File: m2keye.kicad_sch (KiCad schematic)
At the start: 0 parts

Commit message: [#56643] Create buses for interfaces, assign buses to blocks
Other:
- company: (none) -> Antmicro Ltd.
- title: (none) -> Com Express 7 baseboard
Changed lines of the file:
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@@
 (kicad_sch (version 20230121) (generator eeschema)
-  (paper "A4")
+  (paper "A3")
+  (title_block
+    (title "Com Express 7 baseboard")
+    (date "2024-03-22")
+    (rev "1.0.0")
+    (company "Antmicro Ltd.")
+  )
   (hierarchical_label "USB{USB}" (shape input) (at 66.04 81.28 180) (fields_autoplaced)
     (effects (font (size 1.27 1.27)) (justify right))

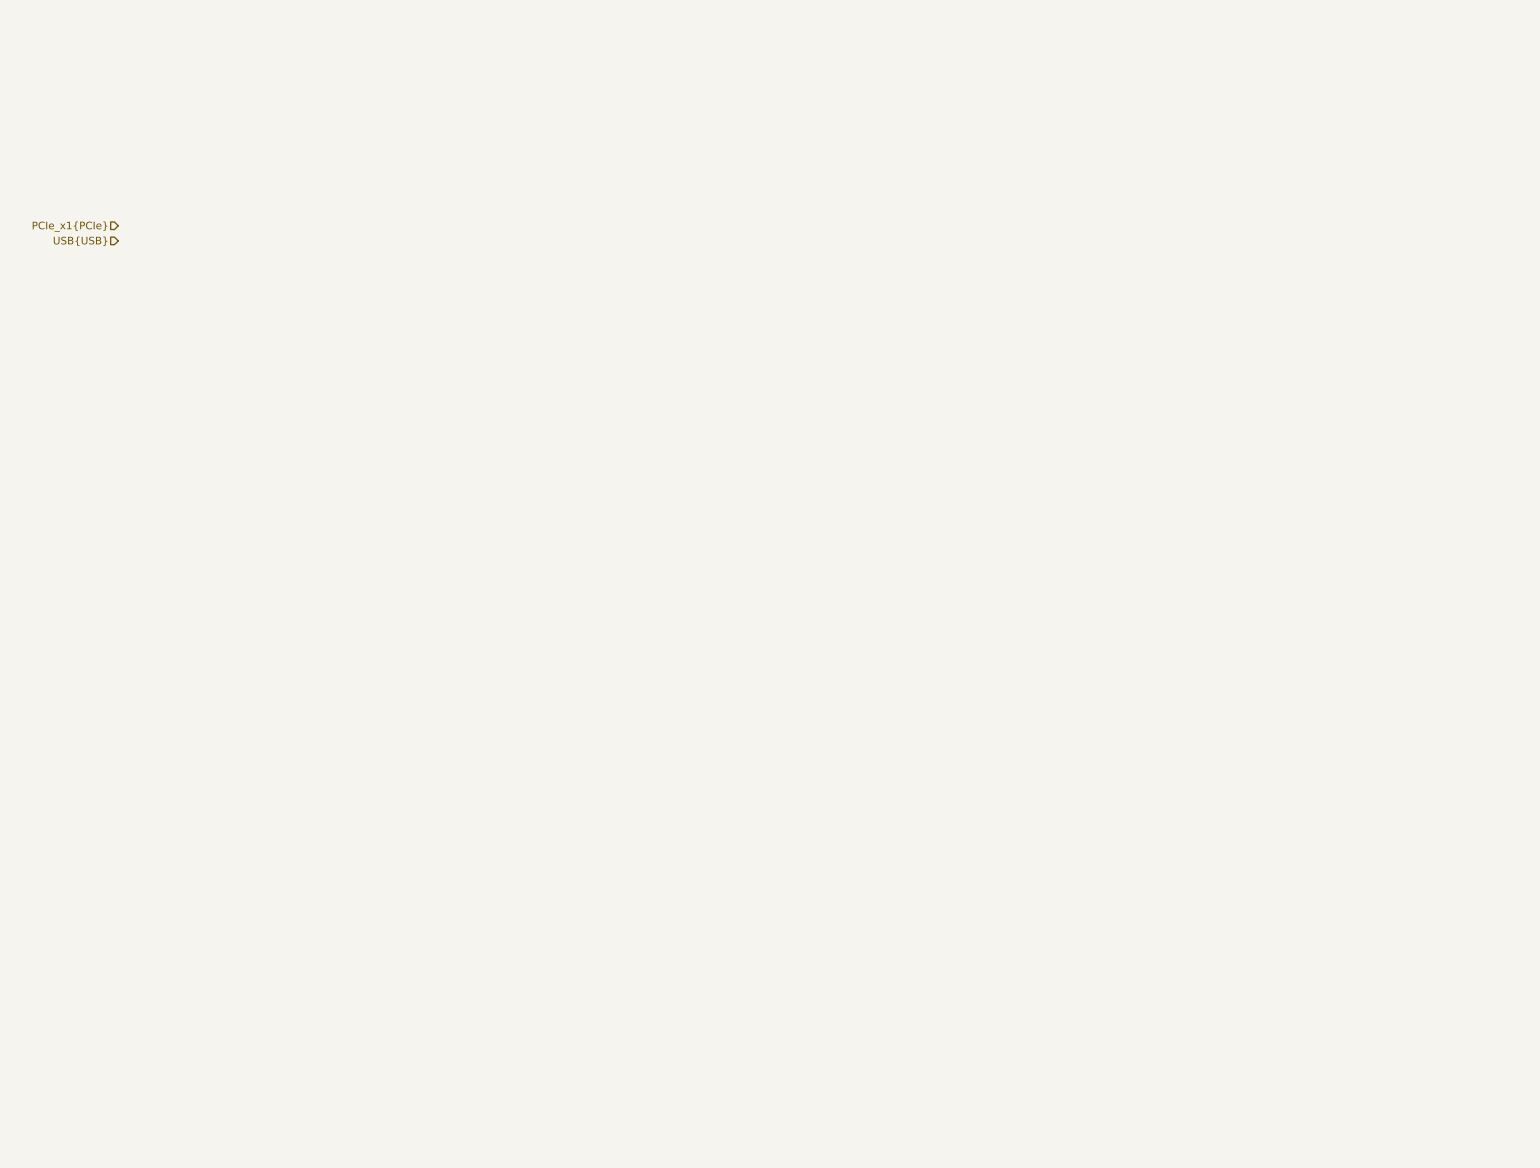
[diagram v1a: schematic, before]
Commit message: [#57056] Create schematics for M.2 and OCuLink connectors
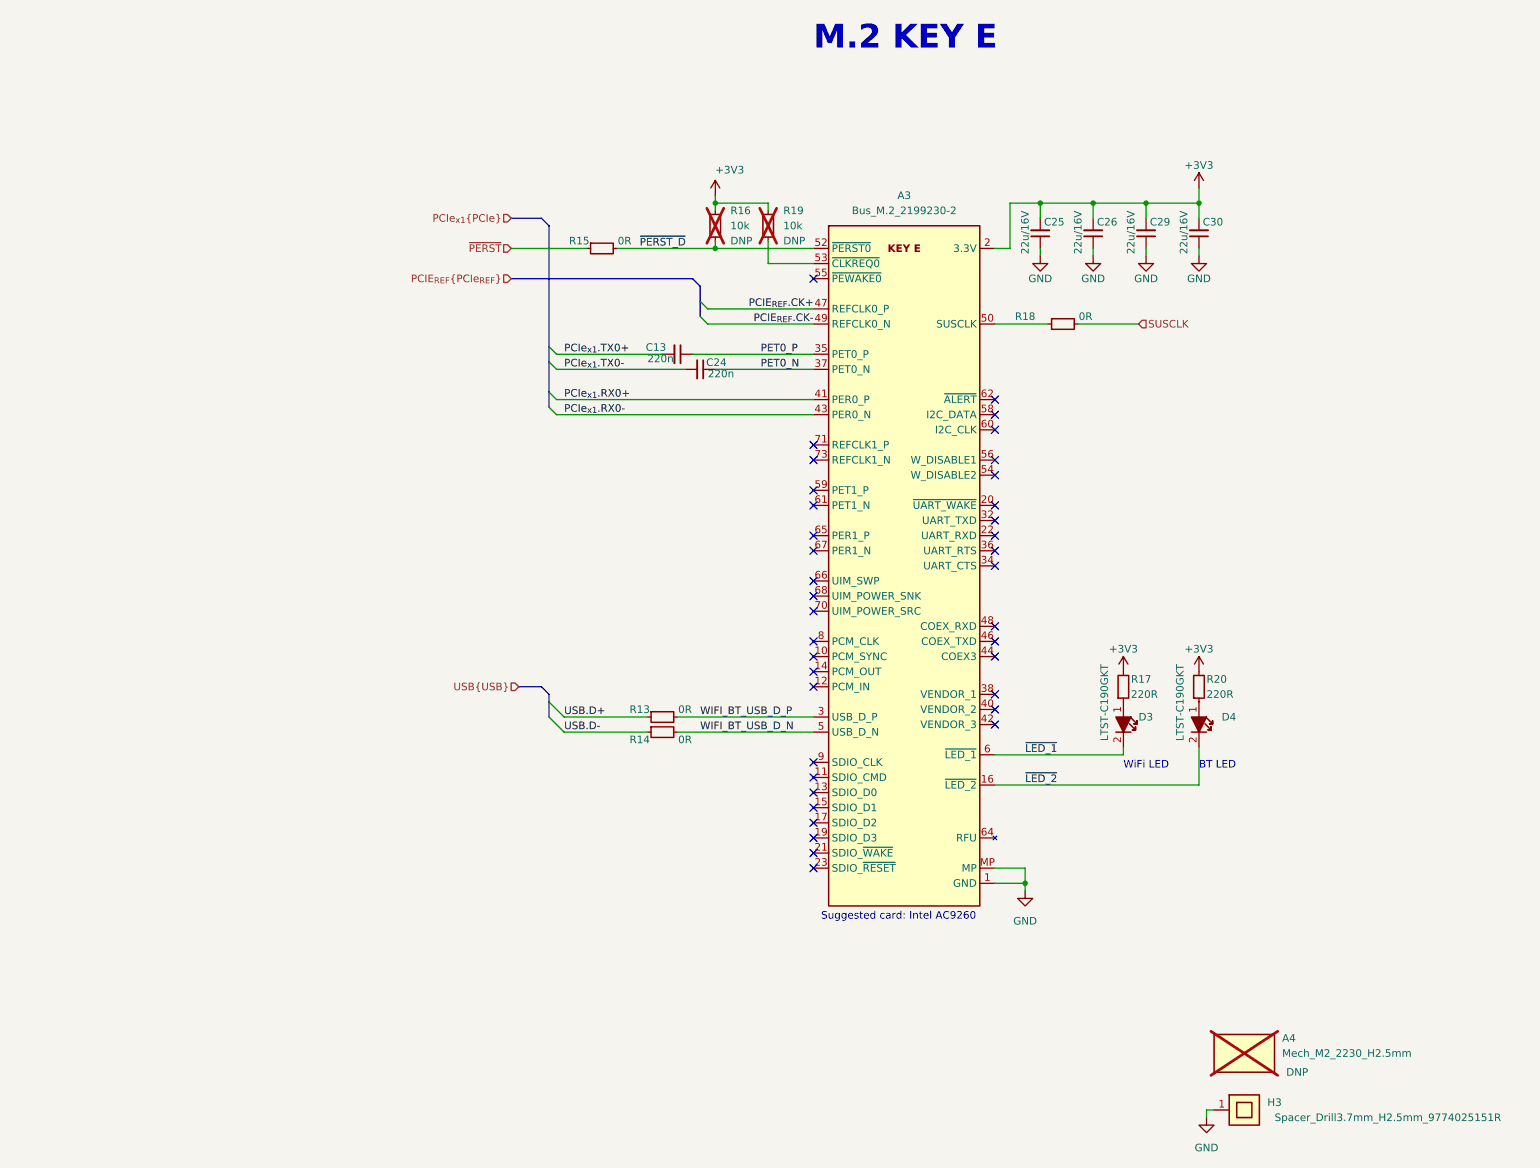
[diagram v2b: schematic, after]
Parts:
- added A3: Bus_M.2_2199230-2, antmicro-footprints:Bus_M.2_Socket_Key_E_TE_2199230-6, symbol antmicroPciConnectors:Bus_M.2_2199230-2
- added A4: Mech_M2_2230_H2.5mm, antmicro-footprints:Mech_M2_2230_H2.5mm, symbol antmicroModules:Mech_M2_2230_H2.5mm
- added C13, C24: C_220n_0402, antmicro-footprints:C_0402_1005Metric, symbol antmicroCapacitors0402:C_220n_0402
- added C25, C26, C29, C30: C_22u_16V_0603, antmicro-footprints:C_0603_1608Metric, symbol antmicroCapacitors0603:C_22u_16V_0603
- added D3, D4: LED_G_0603_LTST-C190GKT, antmicro-footprints:LED_0603_1608Metric_G, symbol antmicroLEDIndicationDiscrete:LED_G_0603_LTST-C190GKT
- added H3: Spacer_Drill3.7mm_H2.5mm_9774025151R, antmicro-footprints:Spacer_Drill3.7mm_H2.5mm_9774025151R, symbol antmicroMechanicalParts:Spacer_Drill3.7mm_H2.5mm_9774025151R
- added R13, R14, R15, R18: R_0R_0402, antmicro-footprints:R_0402_1005Metric, symbol antmicroResistors0402:R_0R_0402
- added R16, R19: R_10k_0402, antmicro-footprints:R_0402_1005Metric, symbol antmicroResistors0402:R_10k_0402
- added R17, R20: R_220R_0402, antmicro-footprints:R_0402_1005Metric, symbol antmicroResistors0402:R_220R_0402
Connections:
- new net: D3.1, R17.1
- new net: A3.50 (SUSCLK), R18.1
- new net: A3.53 (~{CLKREQ0}), R19.1
- new net: D4.1, R20.1
- new net +3V3: A3.2 (3.3V), A3.4 (3.3V), A3.72 (3.3V), A3.74 (3.3V), C25.2, C26.2, C29.2, C30.2, R16.2, R17.2, R19.2, R20.2
- new net GND: A3.1 (GND), A3.18 (GND), A3.33 (GND), A3.39 (GND), A3.45 (GND), A3.51 (GND), A3.57 (GND), A3.63 (GND), A3.69 (GND), A3.7 (GND), A3.75 (GND), A3.MP, C25.1, C26.1, C29.1, C30.1, H3.1
- new net PCIE_{REF}.CK+: A3.47 (REFCLK0_P)
- new net PCIE_{REF}.CK-: A3.49 (REFCLK0_N)
- new net PCIe_{x1}.RX0+: A3.41 (PER0_P)
- new net PCIe_{x1}.RX0-: A3.43 (PER0_N)
- new net PCIe_{x1}.TX0+: C13.2
- new net PCIe_{x1}.TX0-: C24.2
- new net PET0_N: A3.37 (PET0_N), C24.1
- new net PET0_P: A3.35 (PET0_P), C13.1
- new net SUSCLK: R18.2
- new net USB.D+: R13.1
- new net USB.D-: R14.1
- new net WIFI_BT_USB_D_N: A3.5 (USB_D_N), R14.2
- new net WIFI_BT_USB_D_P: A3.3 (USB_D_P), R13.2
- new net ~{LED_1}: A3.6 (~{LED_1}), D3.2
- new net ~{LED_2}: A3.16 (~{LED_2}), D4.2
- new net ~{PERST_D}: A3.52 (~{PERST0}), R15.2, R16.1
- new net ~{PERST}: R15.1
- no-connect marks 0 -> 38
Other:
- note added: "BT LED"
- note added: "M.2 KEY E"
- note added: "Suggested card: Intel AC9260"
- note added: "WiFi LED"

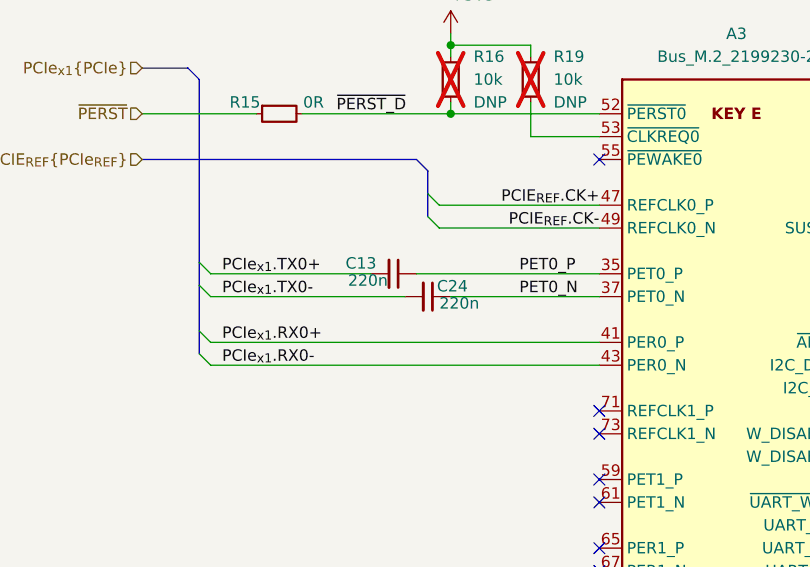
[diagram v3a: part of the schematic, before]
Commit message: [#57056] Remove AC coupling caps on PCIe lines
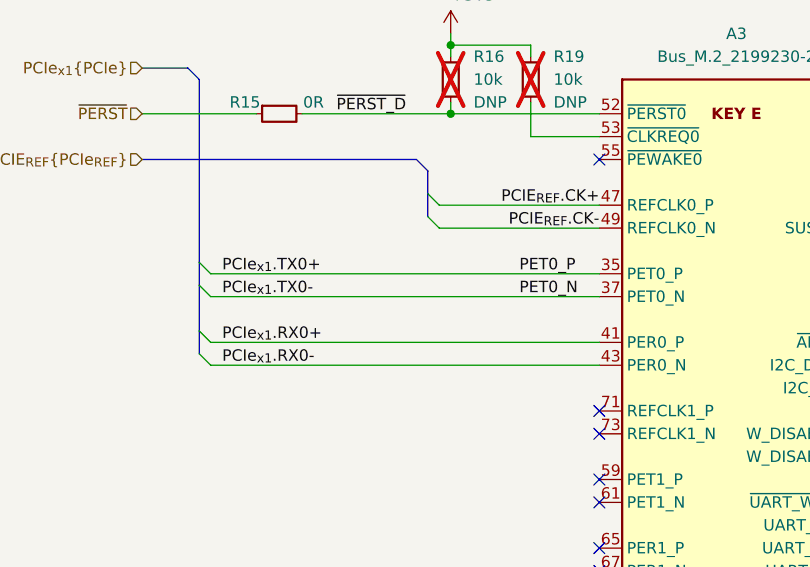
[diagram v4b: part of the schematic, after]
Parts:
- removed C13, C24: C_220n_0402, antmicro-footprints:C_0402_1005Metric, symbol antmicroCapacitors0402:C_220n_0402
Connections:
- net PET0_N is gone; now on net PCIe_{x1}.TX0-: A3.37 (PET0_N)
- net PET0_P is gone; now on net PCIe_{x1}.TX0+: A3.35 (PET0_P)
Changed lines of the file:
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@@
     (stroke (width 0) (type default))
   )
-  (wire (pts (xy 139.7 100.33) (xy 157.48 100.33))
+  (wire (pts (xy 139.7 100.33) (xy 182.88 100.33))
     (stroke (width 0) (type default))
   )
@@
     (stroke (width 0) (type default))
   )
-  (wire (pts (xy 182.88 102.87) (xy 166.37 102.87))
-    (stroke (width 0) (type default))
-  )
   (bus (pts (xy 133.35 156.21) (xy 137.16 156.21))
     (stroke (width 0) (type default))
@@
     (stroke (width 0) (type default))
   )
-  (wire (pts (xy 182.88 100.33) (xy 162.56 100.33))
-    (stroke (width 0) (type default))
-  )
   (wire (pts (xy 182.88 110.49) (xy 139.7 110.49))
     (stroke (width 0) (type default))
@@
     (stroke (width 0) (type default))
   )
-  (wire (pts (xy 139.7 102.87) (xy 161.29 102.87))
+  (wire (pts (xy 139.7 102.87) (xy 182.88 102.87))
     (stroke (width 0) (type default))
   )
@@
     )
   )
-  (symbol (lib_id "antmicroCapacitors0402:C_220n_0402") (at 166.37 102.87 180) (unit 1)
-    (in_bom yes) (on_board yes) (dnp no)
-    (property "Reference" "C24" (at 168.275 100.965 0)
-      (effects (font (size 1.27 1.27)) (justify left bottom))
-    )
-    (property "Value" "C_220n_0402" (at 146.05 92.71 0)
-      (effects (font (size 1.27 1.27) (thickness 0.15)) (justify left bottom) hide)
-    )
-    (property "Footprint" "antmicro-footprints:C_0402_1005Metric" (at 146.05 90.17 0)
-      (effects (font (size 1.27 1.27) (thickness 0.15)) (justify left bottom) hide)
-    )
-    (property "Datasheet" "https://www.yageo.com/en/Chart/Download/pdf/CC0402KRX5R6BB224" (at 146.05 87.63 0)
-      (effects (font (size 1.27 1.27) (thickness 0.15)) (justify left bottom) hide)
-    )
-    (property "Manufacturer" "YAGEO" (at 146.05 82.55 0)
-      (effects (font (size 1.27 1.27) (thickness 0.15)) (justify left bottom) hide)
-    )
-    (property "MPN" "CC0402KRX5R6BB224" (at 146.05 85.09 0)
-      (effects (font (size 1.27 1.27) (thickness 0.15)) (justify left bottom) hide)
-    )
-    (property "Val" "220n" (at 169.545 102.87 0)
-      (effects (font (size 1.27 1.27) (thickness 0.15)) (justify left bottom))
-    )
-    (property "License" "Apache-2.0" (at 146.05 80.01 0)
-      (effects (font (size 1.27 1.27) (thickness 0.15)) (justify left bottom) hide)
-    )
-    (property "Author" "Antmicro" (at 146.05 77.47 0)
-      (effects (font (size 1.27 1.27) (thickness 0.15)) (justify left bottom) hide)
-    )
-    (property "Voltage" "" (at 146.05 74.93 0)
-      (effects (font (size 1.27 1.27)) (justify left bottom) hide)
-    )
-    (property "Dielectric" "" (at 146.05 72.39 0)
-      (effects (font (size 1.27 1.27)) (justify left bottom) hide)
-    )
-    (pin "1")
-    (pin "2")
-    (instances
-      (project "com-express-7-baseboard"
-        (path "/1b8c34da-dad5-4b0b-8c4b-45db766c4dfa/ebb6e8c2-9d30-49b6-83d5-1732977f9e4c"
-          (reference "C24") (unit 1)
-        )
-      )
-    )
-  )
   (symbol (lib_id "antmicroCapacitors0603:C_22u_16V_0603") (at 220.98 82.55 90) (unit 1)
     (in_bom yes) (on_board yes) (dnp no)
@@
         )
       )
-    )
-  )
-  (symbol (lib_id "antmicroCapacitors0402:C_220n_0402") (at 162.56 100.33 180) (unit 1)
-    (in_bom yes) (on_board yes) (dnp no)
-    (property "Reference" "C13" (at 158.115 98.425 0)
-      (effects (font (size 1.27 1.27)) (justify left bottom))
-    )
-    (property "Value" "C_220n_0402" (at 142.24 90.17 0)
-      (effects (font (size 1.27 1.27) (thickness 0.15)) (justify left bottom) hide)
-    )
-    (property "Footprint" "antmicro-footprints:C_0402_1005Metric" (at 142.24 87.63 0)
-      (effects (font (size 1.27 1.27) (thickness 0.15)) (justify left bottom) hide)
-    )
-    (property "Datasheet" "https://www.yageo.com/en/Chart/Download/pdf/CC0402KRX5R6BB224" (at 142.24 85.09 0)
-      (effects (font (size 1.27 1.27) (thickness 0.15)) (justify left bottom) hide)
-    )
-    (property "Manufacturer" "YAGEO" (at 142.24 80.01 0)
-      (effects (font (size 1.27 1.27) (thickness 0.15)) (justify left bottom) hide)
-    )
-    (property "MPN" "CC0402KRX5R6BB224" (at 142.24 82.55 0)
-      (effects (font (size 1.27 1.27) (thickness 0.15)) (justify left bottom) hide)
-    )
-    (property "Val" "220n" (at 159.385 100.33 0)
-      (effects (font (size 1.27 1.27) (thickness 0.15)) (justify left bottom))
-    )
-    (property "License" "Apache-2.0" (at 142.24 77.47 0)
-      (effects (font (size 1.27 1.27) (thickness 0.15)) (justify left bottom) hide)
-    )
-    (property "Author" "Antmicro" (at 142.24 74.93 0)
-      (effects (font (size 1.27 1.27) (thickness 0.15)) (justify left bottom) hide)
-    )
-    (property "Voltage" "" (at 142.24 72.39 0)
-      (effects (font (size 1.27 1.27)) (justify left bottom) hide)
-    )
-    (property "Dielectric" "" (at 142.24 69.85 0)
-      (effects (font (size 1.27 1.27)) (justify left bottom) hide)
-    )
-    (pin "1")
-    (pin "2")
-    (instances
-      (project "com-express-7-baseboard"
-        (path "/1b8c34da-dad5-4b0b-8c4b-45db766c4dfa/ebb6e8c2-9d30-49b6-83d5-1732977f9e4c"
-          (reference "C13") (unit 1)
-        )
-      )

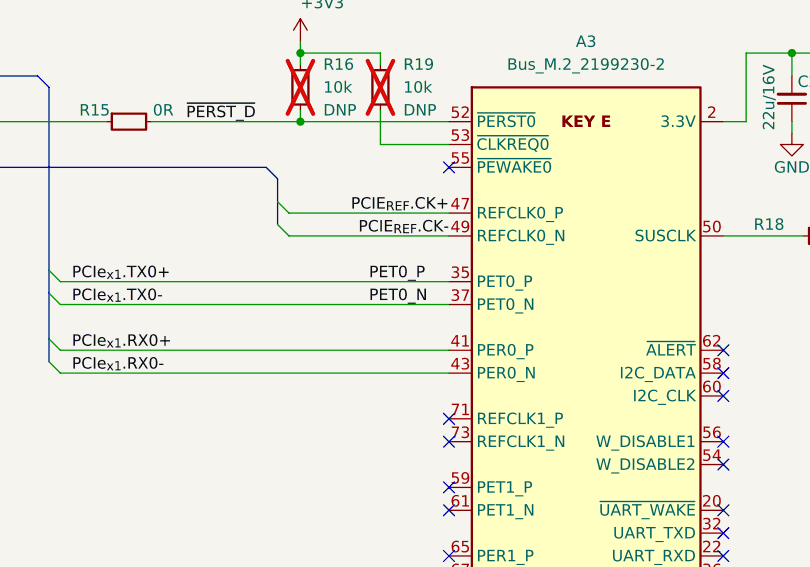
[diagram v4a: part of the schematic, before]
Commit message: [#57056] Add PCIe redriver for OCuLink
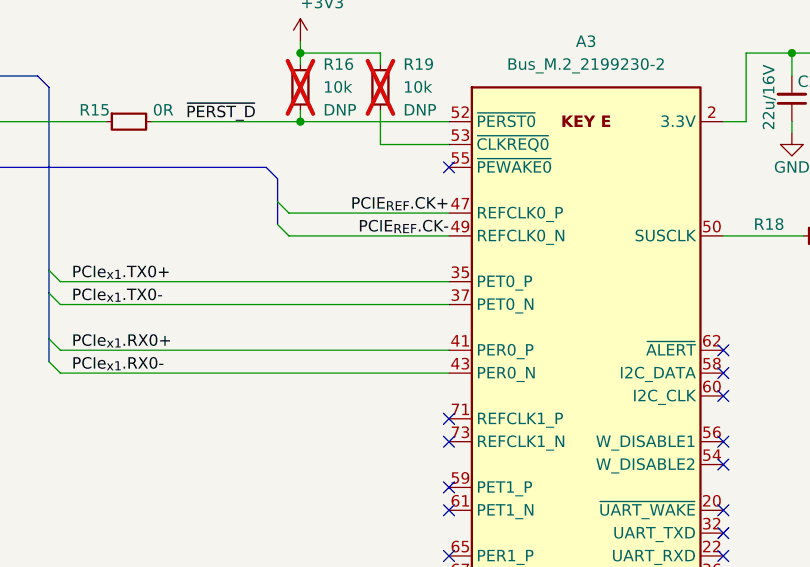
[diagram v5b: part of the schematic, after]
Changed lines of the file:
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@@
-    (effects (font (size 1.27 1.27)) (justify left bottom))
-  )
-  (label "PET0_P" (at 173.99 100.33 0) (fields_autoplaced)
-    (effects (font (size 1.27 1.27)) (justify left bottom))
-  )
-  (label "PET0_N" (at 173.99 102.87 0) (fields_autoplaced)
     (effects (font (size 1.27 1.27)) (justify left bottom))
   )
